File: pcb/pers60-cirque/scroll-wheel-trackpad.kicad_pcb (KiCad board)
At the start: 2 copper layers, 64.8 x 63.5 mm, 11 parts, among them J1 Conn_01x12_Female, J2 Conn_01x12_Female, SW1 RotaryEncoder

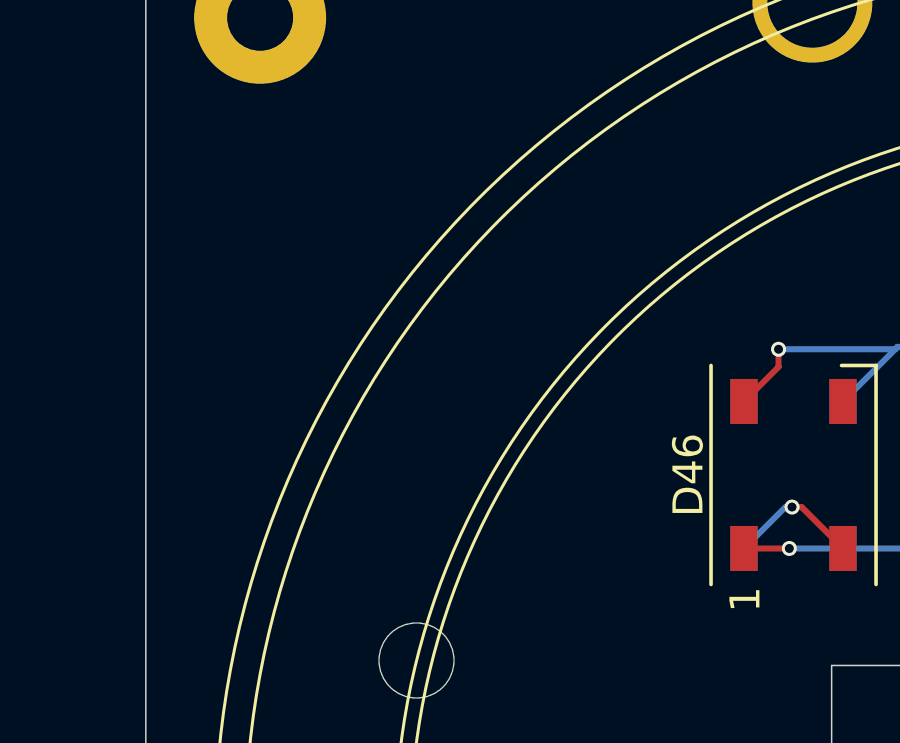
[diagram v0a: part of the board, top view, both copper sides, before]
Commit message: added pmw3360 module, vik logo footprints, and added vik logo to existing pcbs
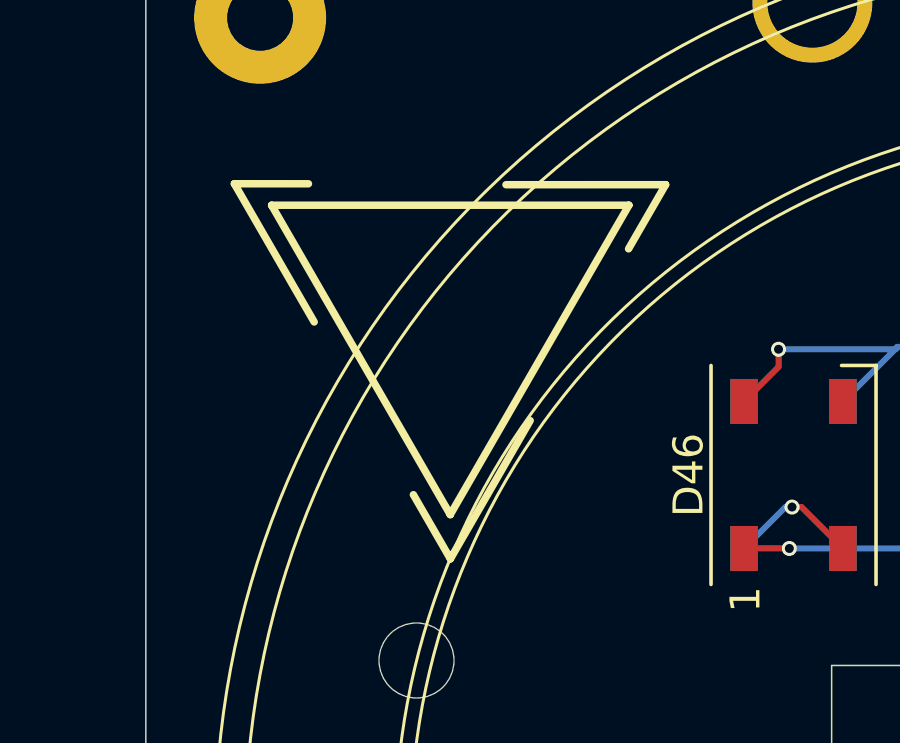
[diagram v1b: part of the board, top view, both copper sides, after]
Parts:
- added REF**: vik-logo-medium, fingerpunch:vik-logo-medium, F.Cu at (152.4, 103.0)
- added REF**: vik-logo-medium, fingerpunch:vik-logo-medium, B.Cu at (152.4, 103.0)
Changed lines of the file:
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@@
+    )
+  )
+  (footprint "fingerpunch:vik-logo-medium" (layer "F.Cu")
+    (at 152.375 103.025)
+    (attr smd)
+    (fp_text reference "REF**" (at -0.05 -6.96 unlocked) (layer "User.1")
+      (effects (font (size 1 1) (thickness 0.15)))
+    )
+    (fp_text value "vik-logo-medium" (at 0.1 9.97 unlocked) (layer "F.Fab")
+      (effects (font (size 1 1) (thickness 0.15)))
+    )
+    (fp_text user "${REFERENCE}" (at 0.3 0.3 unlocked) (layer "F.Fab")
+      (effects (font (size 1 1) (thickness 0.15)))
+    )
+    (fp_line (start 0.012105 6.247404) (end -5.94265 -4.066535) (layer "F.SilkS") (width 0.25))
+    (fp_line (start -5.94265 -4.066535) (end 5.966861 -4.066535) (layer "F.SilkS") (width 0.25))
+    (fp_line (start -7.183542 -4.782401) (end -4.713947 -4.781476) (layer "F.SilkS") (width 0.25))
+    (fp_line (start 7.191148 -4.75075) (end 5.955482 -2.612518) (layer "F.SilkS") (width 0.25))
+    (fp_line (start -4.522363 -0.174502) (end -7.183542 -4.782401) (layer "F.SilkS") (width 0.25))
+    (fp_line (start 2.67707 3.11262) (end 0.017145 7.721245) (layer "F.SilkS") (width 0.25))
+    (fp_line (start 0.017145 7.721245) (end -1.216787 5.582013) (layer "F.SilkS") (width 0.25))
+    (fp_line (start 1.87 -4.75) (end 7.191148 -4.75075) (layer "F.SilkS") (width 0.25))
+    (fp_line (start 5.966861 -4.066535) (end 0.012105 6.247404) (layer "F.SilkS") (width 0.25))
+    (group "" (id 00a67b75-70cc-4b00-ab32-3414ce8a15a5)
+      (members
+        0db5ec6a-55e2-4c2e-8fcd-fdaf9300dbf1
+        5f5eba70-1224-48f8-aa8f-2ab020939ee9
+        7717ba46-01bd-471c-9e3b-f3b4b9913a9c
+        788e9c26-5c24-4c76-a81d-3466a9eeaced
+        7897fc61-0a3e-4f13-a1b3-380253468c79
+        7996afe4-6814-4ec6-8482-c0b2d40a482c
+        9d673692-625c-4e23-966d-2c74a5664f2a
+        bedd1844-d062-44b0-b04a-46b5d6ab1f58
+        f4a87c02-c53e-4620-9eca-87a4ea44028e
+      )
     )
   )
@@
     (pad "14" smd rect (at -4.55 -0.686 90) (size 1.8 2) (layers "B.Cu" "B.Paste" "B.Mask"))
   )
+  (footprint "fingerpunch:vik-logo-medium" (layer "B.Cu")
+    (at 152.375 103 180)
+    (attr smd)
+    (fp_text reference "REF**" (at -0.05 6.96 unlocked) (layer "User.1")
+      (effects (font (size 1 1) (thickness 0.15)))
+    )
+    (fp_text value "vik-logo-medium" (at 0.1 -9.97 unlocked) (layer "B.Fab")
+      (effects (font (size 1 1) (thickness 0.15)) (justify mirror))
+    )
+    (fp_text user "${REFERENCE}" (at 0.3 -0.3 unlocked) (layer "B.Fab")
+      (effects (font (size 1 1) (thickness 0.15)) (justify mirror))
+    )
+    (fp_line (start 0.012105 -6.247404) (end -5.94265 4.066535) (layer "B.SilkS") (width 0.25))
+    (fp_line (start 2.67707 -3.11262) (end 0.017145 -7.721245) (layer "B.SilkS") (width 0.25))
+    (fp_line (start 7.191148 4.75075) (end 5.955482 2.612518) (layer "B.SilkS") (width 0.25))
+    (fp_line (start 0.017145 -7.721245) (end -1.216787 -5.582013) (layer "B.SilkS") (width 0.25))
+    (fp_line (start -5.94265 4.066535) (end 5.966861 4.066535) (layer "B.SilkS") (width 0.25))
+    (fp_line (start 1.87 4.75) (end 7.191148 4.75075) (layer "B.SilkS") (width 0.25))
+    (fp_line (start -4.522363 0.174502) (end -7.183542 4.782401) (layer "B.SilkS") (width 0.25))
+    (fp_line (start 5.966861 4.066535) (end 0.012105 -6.247404) (layer "B.SilkS") (width 0.25))
+    (fp_line (start -7.183542 4.782401) (end -4.713947 4.781476) (layer "B.SilkS") (width 0.25))
+    (group "" (id 4b117c85-84a6-4457-8635-b8642cff05c1)
+      (members
+        083d6bcb-8368-467a-b59f-f4fbf3d41c04
+        11e131ca-d584-457a-bdd9-9f60110c4f88
+        133f3f68-14a8-4e71-8f2f-0abd279407dc
+        7bb7953f-a8aa-4b43-ba44-b10636db4ce1
+        b6166f4b-0584-4d79-bf29-68f4da56c2db
+        b7c17f74-9ee9-4cff-a79f-059363d2a4a8
+        dcd08057-993d-4774-883c-b967098c6ea7
+        e1114032-19cb-46c0-ac57-71d142f1db76
+        fab9016d-ddd0-4286-b964-f4df90c18068
+      )
+    )
+  )
   (gr_line (start 142.24 91.44) (end 142.24 149.86) (layer "Edge.Cuts") (width 0.05))
